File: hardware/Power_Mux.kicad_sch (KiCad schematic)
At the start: 6 parts, among them U4 TPS2117DRLR

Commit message: Update power mux and strain gauge channel schematics
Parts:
- added R58: 16kR, symbol Device:R
- added R60: 4.7kR, symbol Device:R
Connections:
- net MX_GND: now also R60.2
- net PR1: now also R58.2, R60.1
- net VIN_1: now also R58.1
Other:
- note removed: "R1"
- note removed: "R2"
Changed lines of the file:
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@@
-	)
-	(rectangle
-		(start 30.48 58.42)
-		(end 33.02 63.5)
-		(stroke
-			(width 0)
-			(type default)
-		)
-		(fill
-			(type none)
-		)
-	)
-	(rectangle
-		(start 30.48 66.04)
-		(end 33.02 71.12)
-		(stroke
-			(width 0)
-			(type default)
-		)
-		(fill
-			(type none)
-		)
 	)
 	(rectangle
@@
 			(font
 				(size 2.54 2.54)
-			)
-		)
-	)
-	(text "R2"
-		(exclude_from_sim no)
-		(at 31.75 68.834 0)
-		(effects
-			(font
-				(size 1.27 1.27)
-			)
-		)
-	)
-	(text "R1"
-		(exclude_from_sim no)
-		(at 31.75 61.214 0)
-		(effects
-			(font
-				(size 1.27 1.27)
 			)
 		)
@@
 	)
 	(junction
+		(at 31.75 72.39)
+		(diameter 0)
+		(color 0 0 0 0)
+	)
+	(junction
 		(at 88.9 54.61)
 		(diameter 0)
@@
 	)
 	(junction
+		(at 31.75 64.77)
+		(diameter 0)
+		(color 0 0 0 0)
+	)
+	(junction
 		(at 31.75 57.15)
 		(diameter 0)
@@
 	(wire
 		(pts
+			(xy 31.75 72.39) (xy 39.37 72.39)
+		)
+		(stroke
+			(width 0)
+			(type default)
+		)
+	)
+	(wire
+		(pts
 			(xy 39.37 60.96) (xy 39.37 57.15)
 		)
@@
 	(wire
 		(pts
-			(xy 30.48 64.77) (xy 39.37 64.77)
+			(xy 30.48 64.77) (xy 31.75 64.77)
 		)
 		(stroke
@@
 	(wire
 		(pts
+			(xy 31.75 64.77) (xy 39.37 64.77)
+		)
+		(stroke
+			(width 0)
+			(type default)
+		)
+	)
+	(wire
+		(pts
 			(xy 35.56 40.64) (xy 35.56 41.91)
 		)
@@
 	(wire
 		(pts
-			(xy 30.48 72.39) (xy 39.37 72.39)
+			(xy 30.48 72.39) (xy 31.75 72.39)
 		)
 		(stroke
@@
 	(symbol
 		(lib_id "Device:R")
+		(at 31.75 68.58 0)
+		(unit 1)
+		(body_style 1)
+		(exclude_from_sim no)
+		(in_bom yes)
+		(on_board yes)
+		(in_pos_files yes)
+		(dnp no)
+		(property "Reference" "R60"
+			(at 25.146 67.056 0)
+			(show_name no)
+			(do_not_autoplace no)
+			(effects
+				(font
+					(size 1.27 1.27)
+				)
+				(justify left)
+			)
+		)
+		(property "Value" "4.7kR"
+			(at 25.146 69.596 0)
+			(show_name no)
+			(do_not_autoplace no)
+			(effects
+				(font
+					(size 1.27 1.27)
+				)
+				(justify left)
+			)
+		)
+		(property "Footprint" ""
+			(at 29.972 68.58 90)
+			(hide yes)
+			(show_name no)
+			(do_not_autoplace no)
+			(effects
+				(font
+					(size 1.27 1.27)
+				)
+			)
+		)
+		(property "Datasheet" ""
+			(at 31.75 68.58 0)
+			(hide yes)
+			(show_name no)
+			(do_not_autoplace no)
+			(effects
+				(font
+					(size 1.27 1.27)
+				)
+			)
+		)
+		(property "Description" "Resistor"
+			(at 31.75 68.58 0)
+			(hide yes)
+			(show_name no)
+			(do_not_autoplace no)
+			(effects
+				(font
+					(size 1.27 1.27)
+				)
+			)
+		)
+		(pin "1"
+		)
+		(pin "2"
+		)
+		(instances
+			(project "StrainGaugeBoard"
+				(path "/fb459b39-605b-4b65-b2c9-e248812f4f03/ad2265c7-0a96-4914-a6f0-818e23817a72"
+					(reference "R60")
+					(unit 1)
+				)
+			)
+		)
+	)
+	(symbol
+		(lib_id "Device:R")
 		(at 76.2 68.58 0)
 		(unit 1)
@@
 					(unit 1)
 				)
+			)
+		)
+	)
+	(symbol
+		(lib_id "Device:R")
+		(at 31.75 60.96 0)
+		(unit 1)
+		(body_style 1)
+		(exclude_from_sim no)
+		(in_bom yes)
+		(on_board yes)
+		(in_pos_files yes)
+		(dnp no)
+		(property "Reference" "R58"
+			(at 25.4 59.436 0)
+			(show_name no)
+			(do_not_autoplace no)
+			(effects
+				(font
+					(size 1.27 1.27)
+				)
+				(justify left)
+			)
+		)
+		(property "Value" "16kR"
+			(at 25.4 61.976 0)
+			(show_name no)
+			(do_not_autoplace no)
+			(effects
+				(font
+					(size 1.27 1.27)
+				)
+				(justify left)
+			)
+		)
+		(property "Footprint" ""
+			(at 29.972 60.96 90)
+			(hide yes)
+			(show_name no)
+			(do_not_autoplace no)
+			(effects
+				(font
+					(size 1.27 1.27)
+				)
+			)
+		)
+		(property "Datasheet" ""
+			(at 31.75 60.96 0)
+			(hide yes)
+			(show_name no)
+			(do_not_autoplace no)
+			(effects
+				(font
+					(size 1.27 1.27)
+				)
+			)
+		)
+		(property "Description" "Resistor"
+			(at 31.75 60.96 0)
+			(hide yes)
+			(show_name no)
+			(do_not_autoplace no)
+			(effects
+				(font
+					(size 1.27 1.27)
+				)
+			)
+		)
+		(pin "1"
+		)
+		(pin "2"
+		)
+		(instances
+			(project "StrainGaugeBoard"
+				(path "/fb459b39-605b-4b65-b2c9-e248812f4f03/ad2265c7-0a96-4914-a6f0-818e23817a72"
+					(reference "R58")
+					(unit 1)
+				)

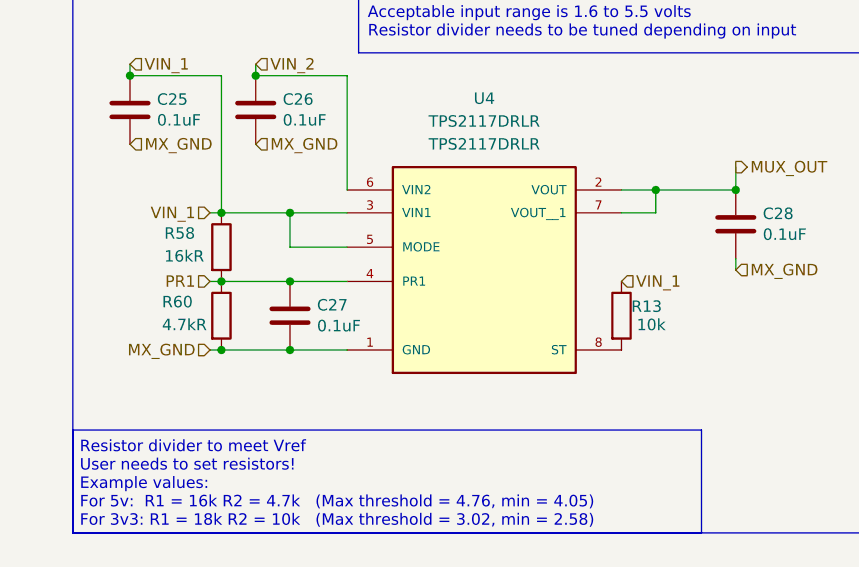
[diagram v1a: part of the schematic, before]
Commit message: Fixed ERC
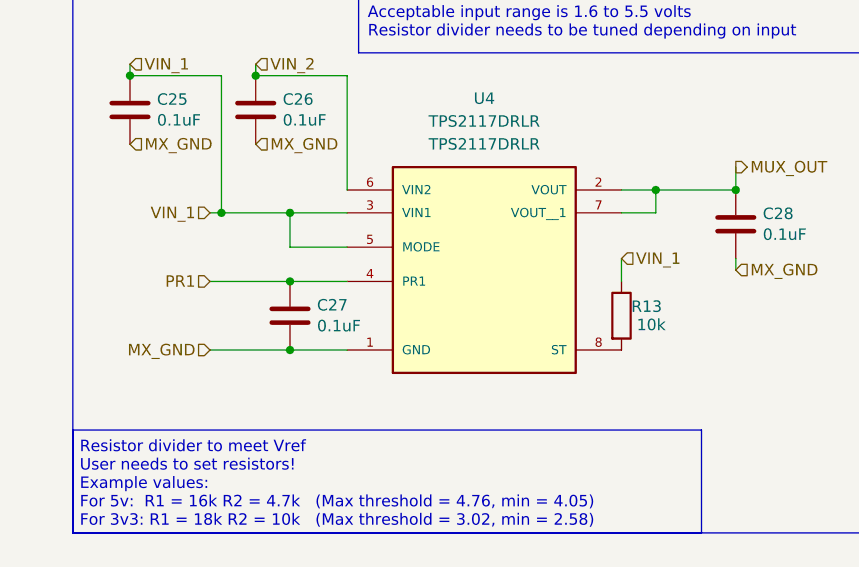
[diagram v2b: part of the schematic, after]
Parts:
- removed R58: 16kR, symbol Device:R
- removed R60: 4.7kR, symbol Device:R
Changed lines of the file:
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@@
 	)
 	(junction
-		(at 31.75 72.39)
+		(at 39.37 57.15)
+		(diameter 0)
+		(color 0 0 0 0)
+	)
+	(junction
+		(at 80.01 54.61)
 		(diameter 0)
 		(color 0 0 0 0)
@@
 	)
 	(junction
-		(at 39.37 57.15)
-		(diameter 0)
-		(color 0 0 0 0)
-	)
-	(junction
-		(at 80.01 54.61)
-		(diameter 0)
-		(color 0 0 0 0)
-	)
-	(junction
-		(at 31.75 64.77)
-		(diameter 0)
-		(color 0 0 0 0)
-	)
-	(junction
 		(at 31.75 57.15)
 		(diameter 0)
@@
 	(wire
 		(pts
-			(xy 31.75 72.39) (xy 39.37 72.39)
-		)
-		(stroke
-			(width 0)
-			(type default)
-		)
-	)
-	(wire
-		(pts
 			(xy 39.37 60.96) (xy 39.37 57.15)
 		)
@@
 	(wire
 		(pts
-			(xy 30.48 64.77) (xy 31.75 64.77)
+			(xy 30.48 64.77) (xy 39.37 64.77)
 		)
 		(stroke
@@
 	(wire
 		(pts
-			(xy 31.75 64.77) (xy 39.37 64.77)
-		)
-		(stroke
-			(width 0)
-			(type default)
-		)
-	)
-	(wire
-		(pts
 			(xy 35.56 40.64) (xy 35.56 41.91)
 		)
@@
 	(wire
 		(pts
+			(xy 76.2 62.23) (xy 76.2 64.77)
+		)
+		(stroke
+			(width 0)
+			(type default)
+		)
+	)
+	(wire
+		(pts
 			(xy 80.01 54.61) (xy 88.9 54.61)
 		)
@@
 	(wire
 		(pts
-			(xy 30.48 72.39) (xy 31.75 72.39)
+			(xy 30.48 72.39) (xy 39.37 72.39)
 		)
 		(stroke
@@
 	(hierarchical_label "VIN_1"
 		(shape input)
-		(at 76.2 64.77 0)
+		(at 76.2 62.23 0)
 		(effects
 			(font
@@
 				(path "/fb459b39-605b-4b65-b2c9-e248812f4f03/ad2265c7-0a96-4914-a6f0-818e23817a72"
 					(reference "C28")
-					(unit 1)
-				)
-			)
-		)
-	)
-	(symbol
-		(lib_id "Device:R")
-		(at 31.75 68.58 0)
-		(unit 1)
-		(body_style 1)
-		(exclude_from_sim no)
-		(in_bom yes)
-		(on_board yes)
-		(in_pos_files yes)
-		(dnp no)
-		(property "Reference" "R60"
-			(at 25.146 67.056 0)
-			(show_name no)
-			(do_not_autoplace no)
-			(effects
-				(font
-					(size 1.27 1.27)
-				)
-				(justify left)
-			)
-		)
-		(property "Value" "4.7kR"
-			(at 25.146 69.596 0)
-			(show_name no)
-			(do_not_autoplace no)
-			(effects
-				(font
-					(size 1.27 1.27)
-				)
-				(justify left)
-			)
-		)
-		(property "Footprint" ""
-			(at 29.972 68.58 90)
-			(hide yes)
-			(show_name no)
-			(do_not_autoplace no)
-			(effects
-				(font
-					(size 1.27 1.27)
-				)
-			)
-		)
-		(property "Datasheet" ""
-			(at 31.75 68.58 0)
-			(hide yes)
-			(show_name no)
-			(do_not_autoplace no)
-			(effects
-				(font
-					(size 1.27 1.27)
-				)
-			)
-		)
-		(property "Description" "Resistor"
-			(at 31.75 68.58 0)
-			(hide yes)
-			(show_name no)
-			(do_not_autoplace no)
-			(effects
-				(font
-					(size 1.27 1.27)
-				)
-			)
-		)
-		(pin "1"
-		)
-		(pin "2"
-		)
-		(instances
-			(project "StrainGaugeBoard"
-				(path "/fb459b39-605b-4b65-b2c9-e248812f4f03/ad2265c7-0a96-4914-a6f0-818e23817a72"
-					(reference "R60")
 					(unit 1)
 				)
@@
 					(unit 1)
 				)
-			)
-		)
-	)
-	(symbol
-		(lib_id "Device:R")
-		(at 31.75 60.96 0)
-		(unit 1)
-		(body_style 1)
-		(exclude_from_sim no)
-		(in_bom yes)
-		(on_board yes)
-		(in_pos_files yes)
-		(dnp no)
-		(property "Reference" "R58"
-			(at 25.4 59.436 0)
-			(show_name no)
-			(do_not_autoplace no)
-			(effects
-				(font
-					(size 1.27 1.27)
-				)
-				(justify left)
-			)
-		)
-		(property "Value" "16kR"
-			(at 25.4 61.976 0)
-			(show_name no)
-			(do_not_autoplace no)
-			(effects
-				(font
-					(size 1.27 1.27)
-				)
-				(justify left)
-			)
-		)
-		(property "Footprint" ""
-			(at 29.972 60.96 90)
-			(hide yes)
-			(show_name no)
-			(do_not_autoplace no)
-			(effects
-				(font
-					(size 1.27 1.27)
-				)
-			)
-		)
-		(property "Datasheet" ""
-			(at 31.75 60.96 0)
-			(hide yes)
-			(show_name no)
-			(do_not_autoplace no)
-			(effects
-				(font
-					(size 1.27 1.27)
-				)
-			)
-		)
-		(property "Description" "Resistor"
-			(at 31.75 60.96 0)
-			(hide yes)
-			(show_name no)
-			(do_not_autoplace no)
-			(effects
-				(font
-					(size 1.27 1.27)
-				)
-			)
-		)
-		(pin "1"
-		)
-		(pin "2"
-		)
-		(instances
-			(project "StrainGaugeBoard"
-				(path "/fb459b39-605b-4b65-b2c9-e248812f4f03/ad2265c7-0a96-4914-a6f0-818e23817a72"
-					(reference "R58")
-					(unit 1)
-				)

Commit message: errors fixed
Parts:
- C33: renamed from C25; value 0.1uF -> 0.1u
- C34: renamed from C26; value 0.1uF -> 0.1u
- C35: renamed from C27; value 0.1uF -> 0.1u
- C36: renamed from C28; value 0.1uF -> 0.1u
- renumbered R13 to R16, U4 to U3
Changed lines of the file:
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@@
 		(in_pos_files yes)
 		(dnp no)
-		(property "Reference" "C28"
+		(property "Reference" "C36"
 			(at 91.8972 57.2516 0)
 			(show_name no)
@@
 			)
 		)
-		(property "Value" "0.1uF"
+		(property "Value" "0.1u"
 			(at 91.8972 59.563 0)
 			(show_name no)
@@
 			)
 			(project "StrainGaugeBoard"
-				(path "/fb459b39-605b-4b65-b2c9-e248812f4f03/ad2265c7-0a96-4914-a6f0-818e23817a72"
-					(reference "C28")
+				(path "/fb459b39-605b-4b65-b2c9-e248812f4f03/277fb226-beeb-42a0-a95e-b53d17001e5c"
+					(reference "C36")
 					(unit 1)
 				)
@@
 		(in_pos_files yes)
 		(dnp no)
-		(property "Reference" "R13"
+		(property "Reference" "R16"
 			(at 78.994 67.564 0)
 			(show_name no)
@@
 			)
 			(project "StrainGaugeBoard"
-				(path "/fb459b39-605b-4b65-b2c9-e248812f4f03/ad2265c7-0a96-4914-a6f0-818e23817a72"
-					(reference "R13")
+				(path "/fb459b39-605b-4b65-b2c9-e248812f4f03/277fb226-beeb-42a0-a95e-b53d17001e5c"
+					(reference "R16")
 					(unit 1)
 				)
@@
 		(in_pos_files yes)
 		(dnp no)
-		(property "Reference" "C25"
+		(property "Reference" "C33"
 			(at 24.5872 44.5516 0)
 			(show_name no)
@@
 			)
 		)
-		(property "Value" "0.1uF"
+		(property "Value" "0.1u"
 			(at 24.5872 46.863 0)
 			(show_name no)
@@
 			)
 			(project "StrainGaugeBoard"
-				(path "/fb459b39-605b-4b65-b2c9-e248812f4f03/ad2265c7-0a96-4914-a6f0-818e23817a72"
-					(reference "C25")
+				(path "/fb459b39-605b-4b65-b2c9-e248812f4f03/277fb226-beeb-42a0-a95e-b53d17001e5c"
+					(reference "C33")
 					(unit 1)
 				)
@@
 		(dnp no)
 		(fields_autoplaced yes)
-		(property "Reference" "U4"
+		(property "Reference" "U3"
 			(at 60.96 44.45 0)
 			(show_name no)
@@
 			)
 			(project "StrainGaugeBoard"
-				(path "/fb459b39-605b-4b65-b2c9-e248812f4f03/ad2265c7-0a96-4914-a6f0-818e23817a72"
-					(reference "U4")
+				(path "/fb459b39-605b-4b65-b2c9-e248812f4f03/277fb226-beeb-42a0-a95e-b53d17001e5c"
+					(reference "U3")
 					(unit 1)
 				)
@@
 		(in_pos_files yes)
 		(dnp no)
-		(property "Reference" "C27"
+		(property "Reference" "C35"
 			(at 42.3672 67.4116 0)
 			(show_name no)
@@
 			)
 		)
-		(property "Value" "0.1uF"
+		(property "Value" "0.1u"
 			(at 42.3672 69.723 0)
 			(show_name no)
@@
 			)
 			(project "StrainGaugeBoard"
-				(path "/fb459b39-605b-4b65-b2c9-e248812f4f03/ad2265c7-0a96-4914-a6f0-818e23817a72"
-					(reference "C27")
+				(path "/fb459b39-605b-4b65-b2c9-e248812f4f03/277fb226-beeb-42a0-a95e-b53d17001e5c"
+					(reference "C35")
 					(unit 1)
 				)
@@
 		(in_pos_files yes)
 		(dnp no)
-		(property "Reference" "C26"
+		(property "Reference" "C34"
 			(at 38.5572 44.5516 0)
 			(show_name no)
@@
 			)
 		)
-		(property "Value" "0.1uF"
+		(property "Value" "0.1u"
 			(at 38.5572 46.863 0)
 			(show_name no)
@@
 			)
 			(project "StrainGaugeBoard"
-				(path "/fb459b39-605b-4b65-b2c9-e248812f4f03/ad2265c7-0a96-4914-a6f0-818e23817a72"
-					(reference "C26")
-					(unit 1)
-				)
+				(path "/fb459b39-605b-4b65-b2c9-e248812f4f03/277fb226-beeb-42a0-a95e-b53d17001e5c"
+					(reference "C34")
+					(unit 1)
+				)

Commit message: whoops forgot to push
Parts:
- C10: renamed from C35; Mfg MLASH168SB7104KTNA01 -> (none)
- C11: renamed from C36; Mfg MLASH168SB7104KTNA01 -> (none)
- C8: renamed from C33; Mfg MLASH168SB7104KTNA01 -> (none)
- C9: renamed from C34; Mfg MLASH168SB7104KTNA01 -> (none)
- U3: symbol mux:TPS2117DRLR -> lhrs_ics:TPS2117DRLR
- renumbered R16 to R5
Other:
- note added: "R1"
- note added: "R2"
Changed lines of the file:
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@@
+	)
+	(rectangle
+		(start 30.48 58.42)
+		(end 33.02 63.5)
+		(stroke
+			(width 0)
+			(type default)
+		)
+		(fill
+			(type none)
+		)
+	)
+	(rectangle
+		(start 30.48 66.04)
+		(end 33.02 71.12)
+		(stroke
+			(width 0)
+			(type default)
+		)
+		(fill
+			(type none)
+		)
 	)
 	(rectangle
@@
 			(font
 				(size 2.54 2.54)
+			)
+		)
+	)
+	(text "R2"
+		(exclude_from_sim no)
+		(at 31.75 68.834 0)
+		(effects
+			(font
+				(size 1.27 1.27)
+			)
+		)
+	)
+	(text "R1"
+		(exclude_from_sim no)
+		(at 31.75 61.214 0)
+		(effects
+			(font
+				(size 1.27 1.27)
 			)
 		)
@@
 	)
 	(junction
+		(at 88.9 54.61)
+		(diameter 0)
+		(color 0 0 0 0)
+	)
+	(junction
 		(at 39.37 57.15)
 		(diameter 0)
@@
 	)
 	(junction
-		(at 88.9 54.61)
-		(diameter 0)
-		(color 0 0 0 0)
-	)
-	(junction
 		(at 31.75 57.15)
 		(diameter 0)
@@
 		(pts
 			(xy 80.01 57.15) (xy 80.01 54.61)
-		)
-		(stroke
-			(width 0)
-			(type default)
-		)
-	)
-	(wire
-		(pts
-			(xy 76.2 62.23) (xy 76.2 64.77)
 		)
 		(stroke
@@
 	(hierarchical_label "VIN_1"
 		(shape input)
-		(at 76.2 62.23 0)
+		(at 76.2 64.77 0)
 		(effects
 			(font
@@
 		(in_pos_files yes)
 		(dnp no)
-		(property "Reference" "C36"
+		(property "Reference" "C11"
 			(at 91.8972 57.2516 0)
 			(show_name no)
@@
 			)
 		)
-		(property "Mfg" "MLASH168SB7104KTNA01"
-			(at 88.9 58.42 0)
-			(hide yes)
-			(show_name no)
-			(do_not_autoplace no)
-			(effects
-				(font
-					(size 1.27 1.27)
-				)
-			)
-		)
 		(pin "1"
 		)
@@
 		)
 		(instances
-			(project "power-mux-block"
+			(project "Power_Mux"
 				(path "/c8207045-8aef-4538-bcc4-1e380c549c2c"
 					(reference "C4")
@@
 			)
 			(project "StrainGaugeBoard"
-				(path "/fb459b39-605b-4b65-b2c9-e248812f4f03/277fb226-beeb-42a0-a95e-b53d17001e5c"
-					(reference "C36")
+				(path "/fb459b39-605b-4b65-b2c9-e248812f4f03/8adc50da-96b4-44c0-ae24-5078d517480f"
+					(reference "C11")
 					(unit 1)
 				)
@@
 		(in_pos_files yes)
 		(dnp no)
-		(property "Reference" "R16"
+		(property "Reference" "R5"
 			(at 78.994 67.564 0)
 			(show_name no)
@@
 		)
 		(instances
-			(project "power-mux-block"
+			(project "Power_Mux"
 				(path "/c8207045-8aef-4538-bcc4-1e380c549c2c"
 					(reference "R1")
@@
 			)
 			(project "StrainGaugeBoard"
-				(path "/fb459b39-605b-4b65-b2c9-e248812f4f03/277fb226-beeb-42a0-a95e-b53d17001e5c"
-					(reference "R16")
+				(path "/fb459b39-605b-4b65-b2c9-e248812f4f03/8adc50da-96b4-44c0-ae24-5078d517480f"
+					(reference "R5")
 					(unit 1)
 				)
@@
 		(in_pos_files yes)
 		(dnp no)
-		(property "Reference" "C33"
+		(property "Reference" "C8"
 			(at 24.5872 44.5516 0)
 			(show_name no)
@@
 			)
 		)
-		(property "Mfg" "MLASH168SB7104KTNA01"
-			(at 21.59 45.72 0)
-			(hide yes)
-			(show_name no)
-			(do_not_autoplace no)
-			(effects
-				(font
-					(size 1.27 1.27)
-				)
-			)
-		)
 		(pin "1"
 		)
@@
 		)
 		(instances
-			(project "power-mux-block"
+			(project "Power_Mux"
 				(path "/c8207045-8aef-4538-bcc4-1e380c549c2c"
 					(reference "C1")
@@
 			)
 			(project "StrainGaugeBoard"
-				(path "/fb459b39-605b-4b65-b2c9-e248812f4f03/277fb226-beeb-42a0-a95e-b53d17001e5c"
-					(reference "C33")
+				(path "/fb459b39-605b-4b65-b2c9-e248812f4f03/8adc50da-96b4-44c0-ae24-5078d517480f"
+					(reference "C8")
 					(unit 1)
 				)
@@
 	)
 	(symbol
-		(lib_id "mux:TPS2117DRLR")
+		(lib_id "lhrs_ics:TPS2117DRLR")
 		(at 60.96 62.23 0)
 		(unit 1)
@@
 			)
 		)
+		(property "P/N" "TPS2117DRLR"
+			(at 60.96 49.53 0)
+			(show_name no)
+			(do_not_autoplace no)
+			(effects
+				(font
+					(size 1.27 1.27)
+				)
+			)
+		)
 		(property "PARTREV" "A"
 			(at 60.96 62.23 0)
@@
 			)
 		)
-		(property "P/N" "TPS2117DRLR"
-			(at 60.96 49.53 0)
-			(show_name no)
-			(do_not_autoplace no)
-			(effects
-				(font
-					(size 1.27 1.27)
-				)
-			)
-		)
 		(pin "6"
 		)
@@
 		)
 		(instances
-			(project ""
+			(project "Power_Mux"
 				(path "/c8207045-8aef-4538-bcc4-1e380c549c2c"
 					(reference "U1")
@@
 			)
 			(project "StrainGaugeBoard"
-				(path "/fb459b39-605b-4b65-b2c9-e248812f4f03/277fb226-beeb-42a0-a95e-b53d17001e5c"
+				(path "/fb459b39-605b-4b65-b2c9-e248812f4f03/8adc50da-96b4-44c0-ae24-5078d517480f"
 					(reference "U3")
 					(unit 1)
@@
 		(in_pos_files yes)
 		(dnp no)
-		(property "Reference" "C35"
+		(property "Reference" "C10"
 			(at 42.3672 67.4116 0)
 			(show_name no)
@@
 			)
 		)
-		(property "Mfg" "MLASH168SB7104KTNA01"
-			(at 39.37 68.58 0)
-			(hide yes)
-			(show_name no)
-			(do_not_autoplace no)
-			(effects
-				(font
-					(size 1.27 1.27)
-				)
-			)
-		)
 		(pin "1"
 		)
@@
 		)
 		(instances
-			(project "power-mux-block"
+			(project "Power_Mux"
 				(path "/c8207045-8aef-4538-bcc4-1e380c549c2c"
 					(reference "C3")
@@
 			)
 			(project "StrainGaugeBoard"
-				(path "/fb459b39-605b-4b65-b2c9-e248812f4f03/277fb226-beeb-42a0-a95e-b53d17001e5c"
-					(reference "C35")
+				(path "/fb459b39-605b-4b65-b2c9-e248812f4f03/8adc50da-96b4-44c0-ae24-5078d517480f"
+					(reference "C10")
 					(unit 1)
 				)
@@
 		(in_pos_files yes)
 		(dnp no)
-		(property "Reference" "C34"
+		(property "Reference" "C9"
 			(at 38.5572 44.5516 0)
 			(show_name no)
@@
 			)
 		)
-		(property "Mfg" "MLASH168SB7104KTNA01"
-			(at 35.56 45.72 0)
-			(hide yes)
-			(show_name no)
-			(do_not_autoplace no)
-			(effects
-				(font
-					(size 1.27 1.27)
-				)
-			)
-		)
 		(pin "1"
 		)
@@
 		)
 		(instances
-			(project "power-mux-block"
+			(project "Power_Mux"
 				(path "/c8207045-8aef-4538-bcc4-1e380c549c2c"
 					(reference "C2")
@@
 			)
 			(project "StrainGaugeBoard"
-				(path "/fb459b39-605b-4b65-b2c9-e248812f4f03/277fb226-beeb-42a0-a95e-b53d17001e5c"
-					(reference "C34")
+				(path "/fb459b39-605b-4b65-b2c9-e248812f4f03/8adc50da-96b4-44c0-ae24-5078d517480f"
+					(reference "C9")
 					(unit 1)
 				)
